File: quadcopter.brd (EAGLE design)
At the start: 137.3 x 137.3 mm, 71 parts, among them J1 AVR_SPI_PRG_6NS, U1 ATMEGA128RFA1, Y2 16MHz

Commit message: commiting new CAM files and new board logos
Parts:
- added U$12: (no value), logos:TROGDOR
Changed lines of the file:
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@@
 <element name="U$10" library="logos" package="DERPY_BATMAN" value="" x="16" y="48"/>
 <element name="U$11" library="logos" package="MUFFIN_MAN" value="" x="39" y="45"/>
+<element name="U$12" library="logos" package="TROGDOR" value="" x="15" y="-2"/>
 </elements>
 <signals>

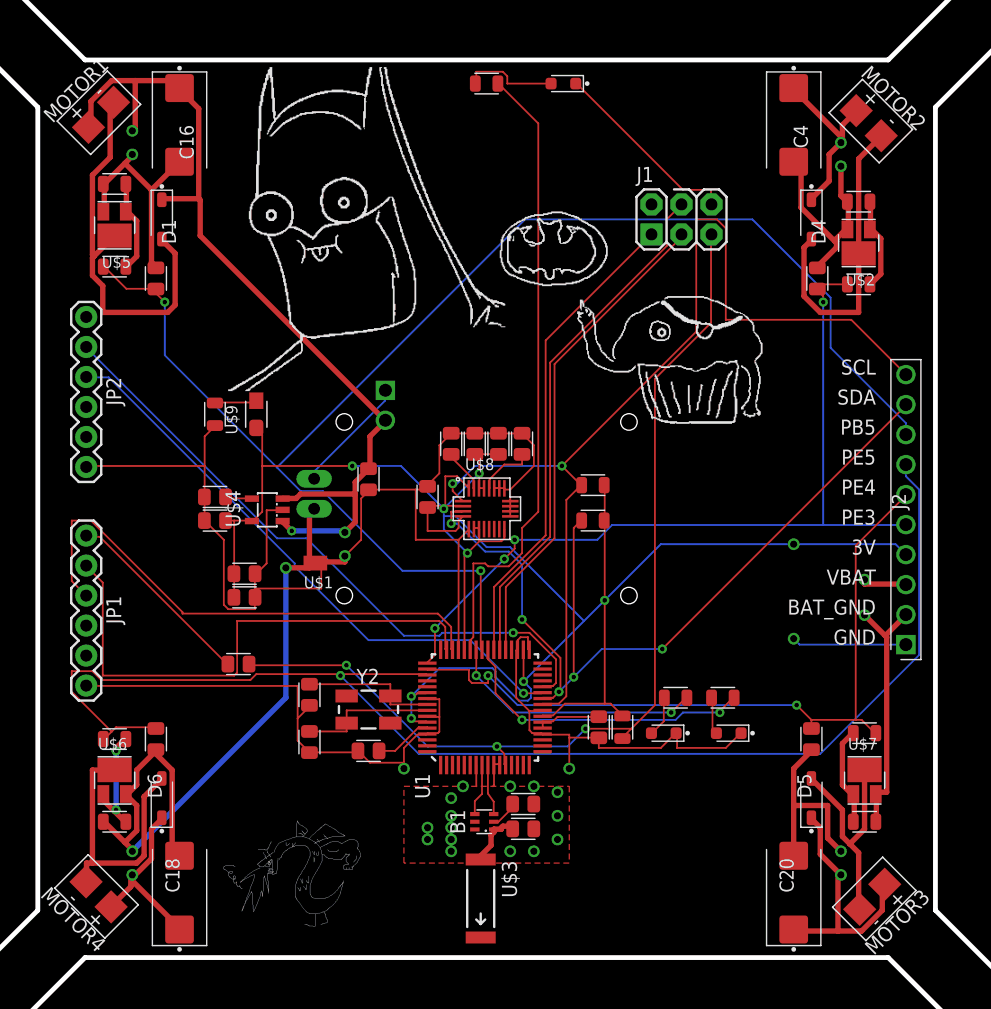
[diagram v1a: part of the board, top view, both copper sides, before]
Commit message: Board ready to be routed with new DRU file
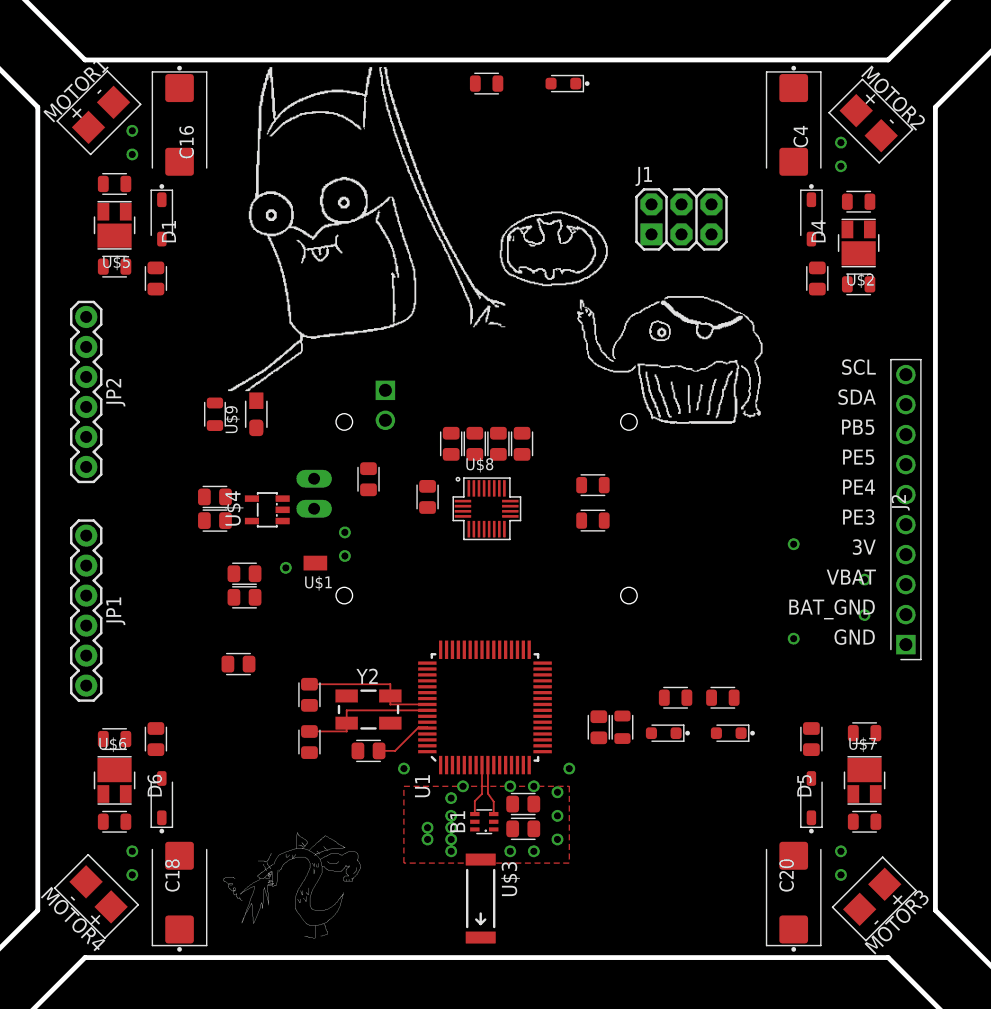
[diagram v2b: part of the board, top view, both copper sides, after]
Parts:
- moved U$12 1.00 mm to (15.0, -3.00)
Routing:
- net GND: track 211.1 -> 0.00 mm
- net 3V: track 178.5 -> 0.00 mm, vias 9 -> 1
- net BAT_GND: track 136.1 -> 0.00 mm
- net VBAT: track 133.5 -> 0.00 mm, vias 7 -> 6
- net PB5: track 124.8 -> 0.00 mm, vias 2 -> 0
- net PE5: track 114.1 -> 0.00 mm, vias 1 -> 0
- net SCL: track 88.1 -> 0.00 mm, vias 2 -> 0
- net RESET: track 83.6 -> 0.00 mm, vias 3 -> 0
- net SDA: track 76.3 -> 0.00 mm, vias 5 -> 0
- net PE3: track 70.3 -> 0.00 mm, vias 4 -> 0
- net PE4: track 63.2 -> 0.00 mm, vias 2 -> 0
- net TX1: track 54.3 -> 0.00 mm, vias 1 -> 0
- net PB7: track 53.9 -> 0.00 mm
- net RX1: track 49.9 -> 0.00 mm, vias 1 -> 0
- net TX0: track 45.6 -> 0.00 mm
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
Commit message: new cam files and rerouted board and stuff
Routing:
- net GND: track 0.00 -> 211.1 mm
- net 3V: track 0.00 -> 178.5 mm, vias 1 -> 9
- net BAT_GND: track 0.00 -> 136.1 mm
- net VBAT: track 0.00 -> 133.5 mm, vias 6 -> 7
- net PB5: track 0.00 -> 124.8 mm, vias 0 -> 2
- net PE5: track 0.00 -> 114.1 mm, vias 0 -> 1
- net SCL: track 0.00 -> 88.1 mm, vias 0 -> 2
- net RESET: track 0.00 -> 83.6 mm, vias 0 -> 3
- net SDA: track 0.00 -> 76.3 mm, vias 0 -> 5
- net PE3: track 0.00 -> 70.3 mm, vias 0 -> 4
- net PE4: track 0.00 -> 63.2 mm, vias 0 -> 2
- net TX1: track 0.00 -> 54.3 mm, vias 0 -> 1
- net PB7: track 0.00 -> 53.9 mm
- net RX1: track 0.00 -> 49.9 mm, vias 0 -> 1
- net TX0: track 0.00 -> 45.6 mm
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
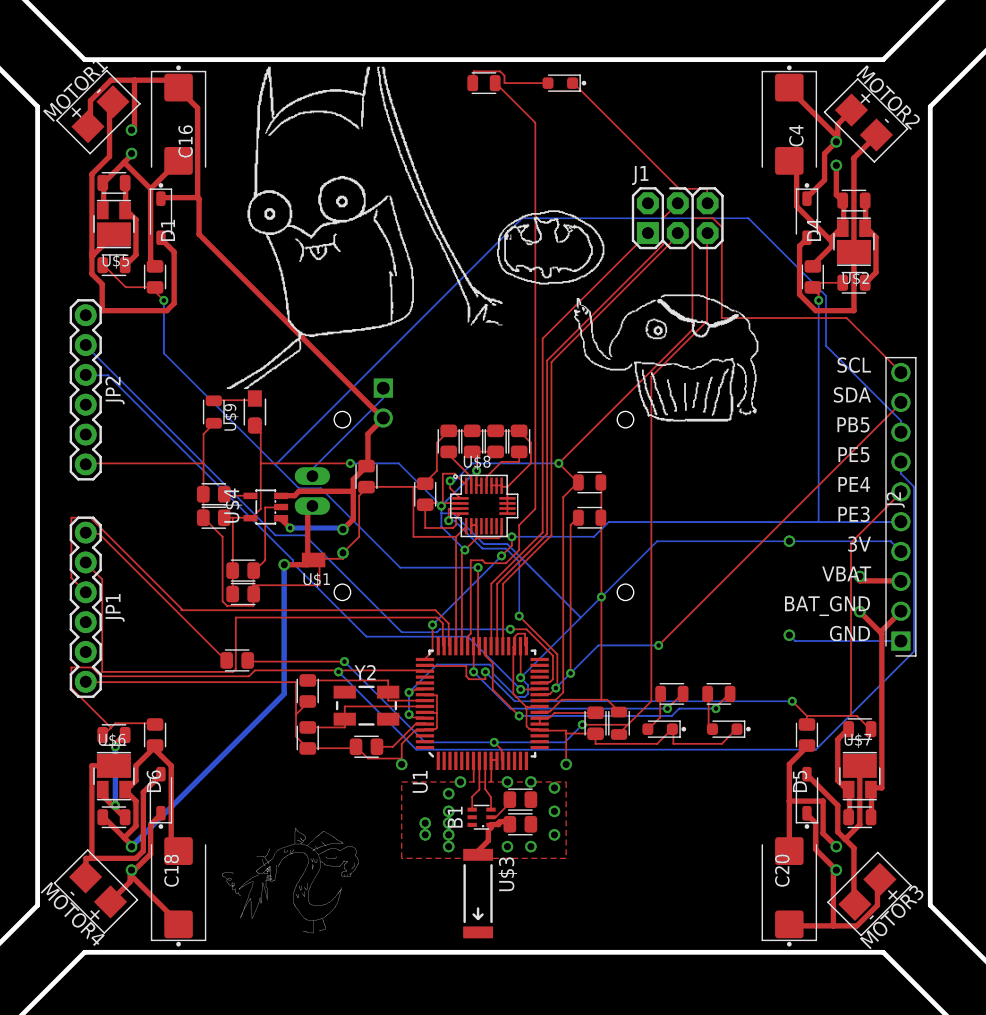
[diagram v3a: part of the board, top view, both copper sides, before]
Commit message: Ripped up everything, manually placed some vias, ready to be routed
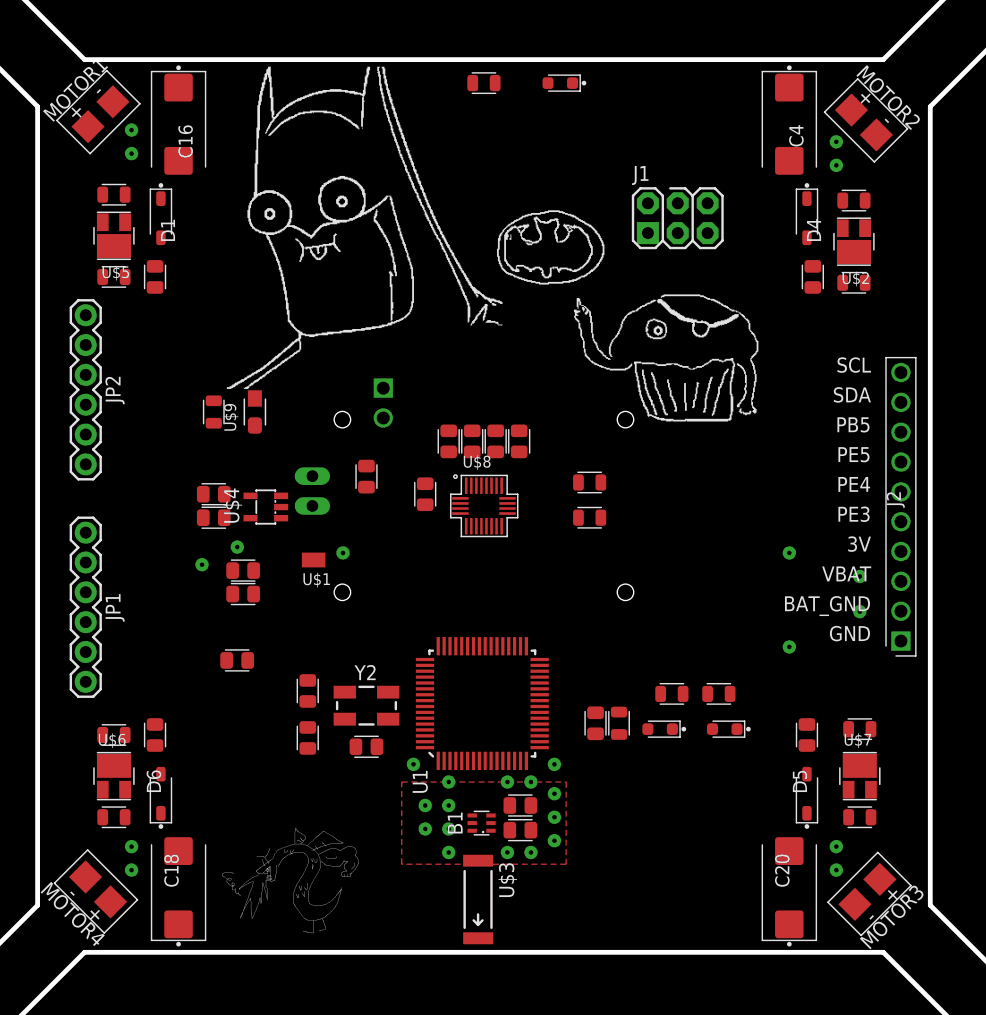
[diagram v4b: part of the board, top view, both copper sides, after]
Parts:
- moved R6 1.00 mm to (6.50, 57.5)
- moved R7 1.00 mm to (6.50, 64.5)
- moved U$5 1.00 mm to (6.50, 61.0)
- moved B1 0.50 mm to (37.8, 11.0)
- moved C10 0.50 mm to (41.1, 10.4)
- moved C9 0.50 mm to (41.1, 12.5)
- moved U$3 0.50 mm to (37.5, 4.50)
- turned C11 to 180 degrees
- turned C12 to 180 degrees
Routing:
- net GND: track 211.1 -> 0.00 mm, vias 19 -> 18
- net 3V: track 178.5 -> 0.00 mm, vias 9 -> 2
- net BAT_GND: track 136.1 -> 0.00 mm, vias 6 -> 5
- net VBAT: track 133.5 -> 0.00 mm, vias 7 -> 5
- net PB5: track 124.8 -> 0.00 mm, vias 2 -> 0
- net PE5: track 114.1 -> 0.00 mm, vias 1 -> 0
- net SCL: track 88.1 -> 0.00 mm, vias 2 -> 0
- net RESET: track 83.6 -> 0.00 mm, vias 3 -> 0
- net SDA: track 76.3 -> 0.00 mm, vias 5 -> 0
- net PE3: track 70.3 -> 0.00 mm, vias 4 -> 0
- net PE4: track 63.2 -> 0.00 mm, vias 2 -> 0
- net TX1: track 54.3 -> 0.00 mm, vias 1 -> 0
- net PB7: track 53.9 -> 0.00 mm
- net RX1: track 49.9 -> 0.00 mm, vias 1 -> 0
- net TX0: track 45.6 -> 0.00 mm
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
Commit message: Changed antenna vias, added routes from balun
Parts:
- moved B1 0.05 mm to (37.9, 11.0)
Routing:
- net N$9: track 0.00 -> 4.87 mm
- net N$10: track 0.00 -> 4.86 mm
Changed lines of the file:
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@@
 <param name="TopRouterVariant" value="1"/>
 <param name="tpViaShape" value="round"/>
-<param name="PrefDir.1" value="*"/>
+<param name="PrefDir.1" value="a"/>
 <param name="PrefDir.2" value="0"/>
 <param name="PrefDir.3" value="0"/>
@@
 <param name="PrefDir.14" value="0"/>
 <param name="PrefDir.15" value="0"/>
-<param name="PrefDir.16" value="-"/>
+<param name="PrefDir.16" value="a"/>
 <param name="cfVia" value="8"/>
 <param name="cfNonPref" value="5"/>
@@
 </autorouter>
 <elements>
-<element name="B1" library="quadparts_prebuilt" package="BALUN" value="BALUN0805" x="37.8" y="11" rot="R90">
-<attribute name="DATASHEET" value="http://katalog.we-online.de/pbs/datasheet/748421245.pdf" x="37.8" y="11" size="1.778" layer="27" rot="R90" display="off"/>
-<attribute name="DIST" value="Digikey" x="37.8" y="11" size="1.778" layer="27" rot="R90" display="off"/>
-<attribute name="DISTPN" value="732-2230-6-ND" x="37.8" y="11" size="1.778" layer="27" rot="R90" display="off"/>
-<attribute name="MFR" value="Wurth Electronics Inc" x="37.8" y="11" size="1.778" layer="27" rot="R90" display="off"/>
-<attribute name="MPN" value="748421245" x="37.8" y="11" size="1.778" layer="27" rot="R90" display="off"/>
-<attribute name="PRICE" value="2.63" x="37.8" y="11" size="1.778" layer="27" rot="R90" display="off"/>
+<element name="B1" library="quadparts_prebuilt" package="BALUN" value="BALUN0805" x="37.85" y="11" rot="R90">
+<attribute name="DATASHEET" value="http://katalog.we-online.de/pbs/datasheet/748421245.pdf" x="37.85" y="11" size="1.778" layer="27" rot="R90" display="off"/>
+<attribute name="DIST" value="Digikey" x="37.85" y="11" size="1.778" layer="27" rot="R90" display="off"/>
+<attribute name="DISTPN" value="732-2230-6-ND" x="37.85" y="11" size="1.778" layer="27" rot="R90" display="off"/>
+<attribute name="MFR" value="Wurth Electronics Inc" x="37.85" y="11" size="1.778" layer="27" rot="R90" display="off"/>
+<attribute name="MPN" value="748421245" x="37.85" y="11" size="1.778" layer="27" rot="R90" display="off"/>
+<attribute name="PRICE" value="2.63" x="37.85" y="11" size="1.778" layer="27" rot="R90" display="off"/>
 </element>
 <element name="BATT1" library="quadparts_prebuilt" package="BATTERY-W/HOLDER-380MAH-HUBSAN" value="BATTERY-HUBSAN-W/HOLDER" x="38" y="38" rot="MR270">
@@
 <attribute name="MPN" value="X4-H107C-8-in-1" x="38" y="38" size="1.778" layer="28" rot="MR270" display="off"/>
 </element>
-<element name="C10" library="quadparts_prebuilt" package="CAPC2012X140_HS" value="0.75pF" x="41.1" y="10.4">
-<attribute name="DIST" value="Digikey" x="41.1" y="10.4" size="1.778" layer="27" display="off"/>
-<attribute name="DISTPN" value="490-3585-1-ND" x="41.1" y="10.4" size="1.778" layer="27" display="off"/>
-<attribute name="MFR" value="Murata Electronics North America" x="41.1" y="10.4" size="1.778" layer="27" display="off"/>
-<attribute name="MPN" value="GQM2195C2AR75CB01D" x="41.1" y="10.4" size="1.778" layer="27" display="off"/>
+<element name="C10" library="quadparts_prebuilt" package="CAPC2012X140_HS" value="0.75pF" x="41.15" y="10.4">
+<attribute name="DIST" value="Digikey" x="41.15" y="10.4" size="1.778" layer="27" display="off"/>
+<attribute name="DISTPN" value="490-3585-1-ND" x="41.15" y="10.4" size="1.778" layer="27" display="off"/>
+<attribute name="MFR" value="Murata Electronics North America" x="41.15" y="10.4" size="1.778" layer="27" display="off"/>
+<attribute name="MPN" value="GQM2195C2AR75CB01D" x="41.15" y="10.4" size="1.778" layer="27" display="off"/>
 </element>
 <element name="C11" library="quadparts_prebuilt" package="CAPC2012X140_HS" value="1uF" x="17.5" y="30.5" rot="R180">
@@
 <attribute name="MPN" value="GRM21BR71H105KA12L" x="28" y="17.5" size="1.778" layer="27" rot="R180" display="off"/>
 </element>
-<element name="C9" library="quadparts_prebuilt" package="CAPC2012X140_HS" value="22pF" x="41.1" y="12.5">
-<attribute name="DIST" value="Digikey" x="41.1" y="12.5" size="1.778" layer="27" display="off"/>
-<attribute name="DISTPN" value="490-5534-1-ND" x="41.1" y="12.5" size="1.778" layer="27" display="off"/>
-<attribute name="MFR" value="Murata Electronics North America" x="41.1" y="12.5" size="1.778" layer="27" display="off"/>
-<attribute name="MPN" value="GRM21A5C2E220JW01D" x="41.1" y="12.5" size="1.778" layer="27" display="off"/>
+<element name="C9" library="quadparts_prebuilt" package="CAPC2012X140_HS" value="22pF" x="41.15" y="12.5">
+<attribute name="DIST" value="Digikey" x="41.15" y="12.5" size="1.778" layer="27" display="off"/>
+<attribute name="DISTPN" value="490-5534-1-ND" x="41.15" y="12.5" size="1.778" layer="27" display="off"/>
+<attribute name="MFR" value="Murata Electronics North America" x="41.15" y="12.5" size="1.778" layer="27" display="off"/>
+<attribute name="MPN" value="GRM21A5C2E220JW01D" x="41.15" y="12.5" size="1.778" layer="27" display="off"/>
 </element>
 <element name="D1" library="quadparts_prebuilt" package="SOD3716X135_HS" value="360mV" x="10.5" y="62.5" rot="R270">
@@
 </polygon>
 <contactref element="U$1" pad="L"/>
-<via x="35" y="14.5" extent="1-16" drill="0.381" diameter="0.381"/>
-<via x="35" y="12.5" extent="1-16" drill="0.381" diameter="0.381"/>
-<via x="33" y="12.5" extent="1-16" drill="0.381" diameter="0.381"/>
-<via x="33" y="10.5" extent="1-16" drill="0.381" diameter="0.381"/>
-<via x="35" y="10.5" extent="1-16" drill="0.381" diameter="0.381"/>
-<via x="35" y="8.5" extent="1-16" drill="0.381" diameter="0.381"/>
+<via x="35" y="12.75" extent="1-16" drill="0.381" diameter="0.381"/>
+<via x="35" y="11.25" extent="1-16" drill="0.381" diameter="0.381"/>
+<via x="33.5" y="12.75" extent="1-16" drill="0.381" diameter="0.381"/>
+<via x="33.5" y="11.25" extent="1-16" drill="0.381" diameter="0.381"/>
+<via x="35" y="9.75" extent="1-16" drill="0.381" diameter="0.381"/>
+<via x="35" y="8.25" extent="1-16" drill="0.381" diameter="0.381"/>
 <via x="40" y="8.5" extent="1-16" drill="0.381" diameter="0.381"/>
 <via x="42" y="8.5" extent="1-16" drill="0.381" diameter="0.381"/>
@@
 <via x="14" y="33" extent="1-16" drill="0.381" diameter="0.381"/>
 <via x="64" y="26" extent="1-16" drill="0.381" diameter="0.381"/>
+<via x="35" y="14.25" extent="1-16" drill="0.381"/>
+<via x="33.5" y="9.75" extent="1-16" drill="0.381"/>
 <wire x1="57.04" y1="63.77" x2="45.545" y2="74" width="0" layer="19" extent="1-1"/>
 <wire x1="39.11" y1="16.299" x2="40" y2="14.5" width="0" layer="19" extent="1-1"/>
@@
 <contactref element="U1" pad="9"/>
 <contactref element="B1" pad="3"/>
-<wire x1="38.6" y1="11.65" x2="38.11" y2="16.299" width="0" layer="19" extent="1-1"/>
+<wire x1="38.11" y1="16.299" x2="38.11" y2="13.59" width="0.1524" layer="1"/>
+<wire x1="38.11" y1="13.59" x2="38.65" y2="13" width="0.1524" layer="1"/>
+<wire x1="38.65" y1="13" x2="38.65" y2="11.65" width="0.1524" layer="1"/>
 </signal>
 <signal name="N$11">
 <contactref element="C9" pad="1"/>
 <contactref element="B1" pad="2"/>
-<wire x1="38.6" y1="11" x2="40.205" y2="12.5" width="0" layer="19" extent="1-1"/>
+<wire x1="38.65" y1="11" x2="40.255" y2="12.5" width="0" layer="19" extent="1-1"/>
 </signal>
 <signal name="N$9">
 <contactref element="U1" pad="8"/>
 <contactref element="B1" pad="4"/>
-<wire x1="37" y1="11.65" x2="37.61" y2="16.299" width="0" layer="19" extent="1-1"/>
+<wire x1="37.61" y1="16.299" x2="37.61" y2="13.61" width="0.1524" layer="1"/>
+<wire x1="37.61" y1="13.61" x2="37.05" y2="13" width="0.1524" layer="1"/>
+<wire x1="37.05" y1="13" x2="37.05" y2="11.65" width="0.1524" layer="1"/>
 </signal>
 <signal name="N$12" class="1">
@@
 <contactref element="U$3" pad="FEED"/>
 <contactref element="C10" pad="1"/>
-<wire x1="40.205" y1="10.4" x2="38.6" y2="10.35" width="0" layer="19" extent="1-1"/>
-<wire x1="37.5" y1="7.802" x2="38.6" y2="10.35" width="0" layer="19" extent="1-1"/>
+<wire x1="40.255" y1="10.4" x2="38.65" y2="10.35" width="0" layer="19" extent="1-1"/>
+<wire x1="37.5" y1="7.802" x2="38.65" y2="10.35" width="0" layer="19" extent="1-1"/>
 </signal>
 <signal name="N$13">

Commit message: Manually routed crystal, fixed motor driver filters.
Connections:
- net BAT_GND: now also R1.1, R10.1, R6.1, R8.1; no longer C1.2, C15.2, C17.2, C19.2
- net FILTERED1: now also C15.2; no longer R6.2
- net FILTERED2: now also C1.1; no longer R1.2
- net FILTERED3: now also C19.2; no longer R10.2
- net FILTERED4: now also C17.2; no longer R8.2
- net PB5: now also R6.2; no longer R6.1
- net PE3: now also C1.2, R1.2; no longer C1.1, R1.1
- net PE4: now also R10.2; no longer R10.1
- net PE5: now also R8.2; no longer R8.1
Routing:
- net GND: track 0.00 -> 14.5 mm
- net N$5: track 0.00 -> 11.8 mm
- net N$4: track 0.00 -> 11.7 mm
- net N$8: track 0.00 -> 4.88 mm

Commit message: Routed board, CAM files
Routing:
- net GND: track 14.5 -> 212.5 mm, vias 20 -> 22
- net BAT_GND: track 0.00 -> 168.1 mm, vias 5 -> 7
- net 3V: track 0.00 -> 156.0 mm, vias 2 -> 6
- net PB5: track 0.00 -> 136.3 mm, vias 0 -> 2
- net VBAT: track 0.00 -> 130.5 mm
- net PE5: track 0.00 -> 91.5 mm, vias 0 -> 1
- net RESET: track 0.00 -> 87.5 mm, vias 0 -> 3
- net PE3: track 0.00 -> 77.2 mm, vias 0 -> 1
- net RX1: track 0.00 -> 66.7 mm, vias 0 -> 3
- net PE4: track 0.00 -> 64.7 mm, vias 0 -> 2
- net SCL: track 0.00 -> 64.6 mm, vias 0 -> 2
- net SDA: track 0.00 -> 64.5 mm, vias 0 -> 4
- net TX1: track 0.00 -> 60.3 mm, vias 0 -> 1
- net MOSI: track 0.00 -> 57.4 mm, vias 0 -> 2
- net PB7: track 0.00 -> 52.0 mm, vias 0 -> 2
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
